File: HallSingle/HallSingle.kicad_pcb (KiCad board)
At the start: 2 copper layers, 12 x 24 mm, 11 parts, among them J1 Conn_01x03, U1 SS49E, U2 TS331ILT

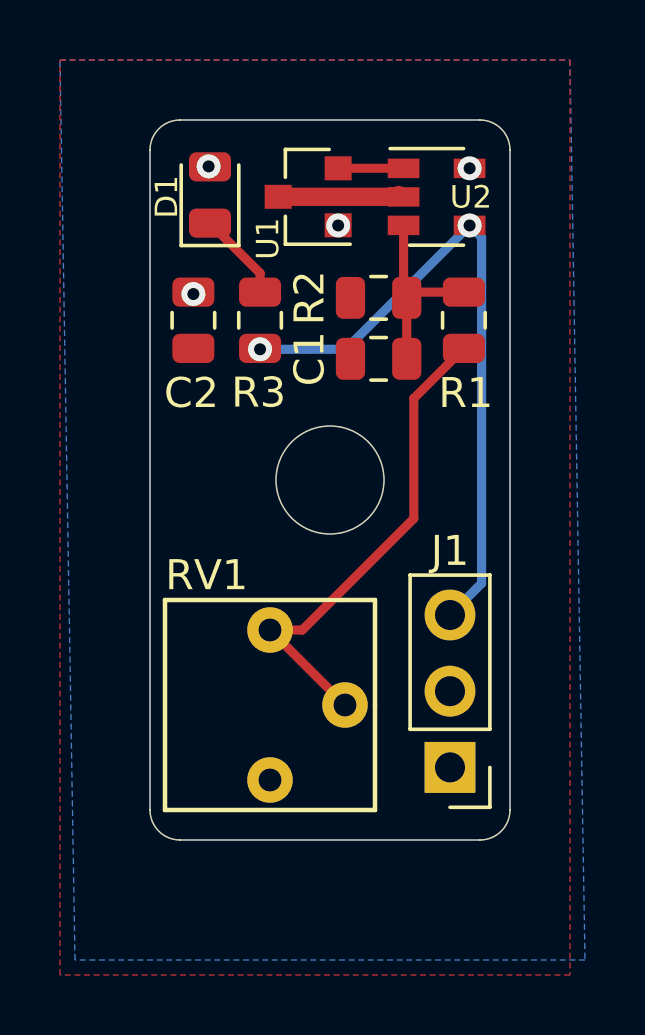
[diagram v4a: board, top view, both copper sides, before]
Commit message: actually reduce the pcb size this time....
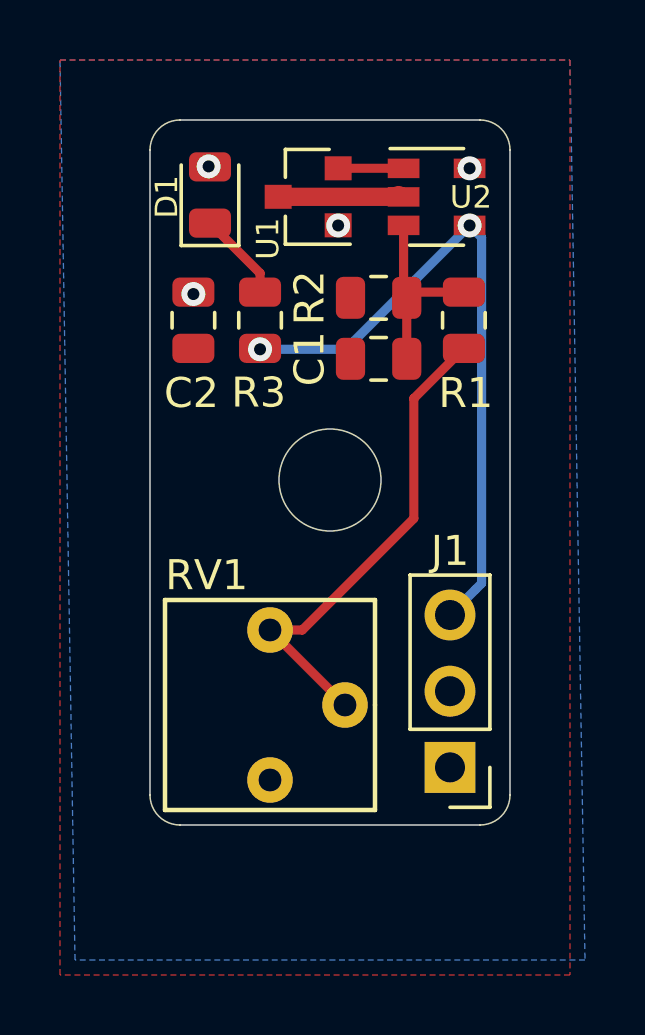
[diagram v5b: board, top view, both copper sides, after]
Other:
- board size 12 x 24 mm -> 12 x 23.5 mm
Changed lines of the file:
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@@
     (effects (font (size 1 1) (thickness 0.15)) (justify mirror))
   )
-  (gr_arc (start 139 80) (end 138 80) (angle -90) (layer Edge.Cuts) (width 0.05))
-  (gr_arc (start 149 80) (end 149 81) (angle -90) (layer Edge.Cuts) (width 0.05))
+  (gr_arc (start 139 79.5) (end 138 79.5) (angle -90) (layer Edge.Cuts) (width 0.05))
+  (gr_arc (start 149 79.5) (end 149 80.5) (angle -90) (layer Edge.Cuts) (width 0.05))
   (gr_arc (start 149 58) (end 150 58) (angle -90) (layer Edge.Cuts) (width 0.05))
   (gr_arc (start 139 58) (end 139 57) (angle -90) (layer Edge.Cuts) (width 0.05))
-  (gr_line (start 138 58) (end 138 80) (layer Edge.Cuts) (width 0.05))
-  (gr_line (start 149 81) (end 139 81) (layer Edge.Cuts) (width 0.05))
-  (gr_circle (center 144 69) (end 145.8 69) (layer Edge.Cuts) (width 0.05))
-  (gr_line (start 150 58) (end 150 80) (layer Edge.Cuts) (width 0.05))
+  (gr_line (start 138 58) (end 138 79.5) (layer Edge.Cuts) (width 0.05))
+  (gr_line (start 149 80.5) (end 139 80.5) (layer Edge.Cuts) (width 0.05))
+  (gr_circle (center 144 69) (end 145.7 69) (layer Edge.Cuts) (width 0.05))
+  (gr_line (start 150 58) (end 150 79.5) (layer Edge.Cuts) (width 0.05))
   (gr_line (start 139 57) (end 149 57) (layer Edge.Cuts) (width 0.05))
   (segment (start 146.284 59.5) (end 146.347 59.563) (width 0.6096) (layer F.Cu) (net 1))
@@
   (via (at 139.954 58.547) (size 0.8) (drill 0.4) (layers F.Cu B.Cu) (net 3))
   (via (at 144.272 60.5155) (size 0.8) (drill 0.4) (layers F.Cu B.Cu) (net 3))
-  (segment (start 143.07763 74) (end 142 74) (width 0.3048) (layer F.Cu) (net 6))
   (segment (start 141.6685 62.106) (end 140 60.4375) (width 0.3048) (layer F.Cu) (net 4))
   (segment (start 141.6685 62.738) (end 141.6685 62.106) (width 0.3048) (layer F.Cu) (net 4))
@@
   (segment (start 149.053499 72.446501) (end 148.849999 72.650001) (width 0.3048) (layer B.Cu) (net 5))
   (segment (start 148.6535 60.5155) (end 149.053499 60.915499) (width 0.3048) (layer B.Cu) (net 5))
+  (segment (start 143.07763 74) (end 142 74) (width 0.3048) (layer F.Cu) (net 6))
   (segment (start 148.463 64.613) (end 146.794399 66.281601) (width 0.3048) (layer F.Cu) (net 6))
   (segment (start 146.794399 66.281601) (end 146.794399 70.283231) (width 0.3048) (layer F.Cu) (net 6))

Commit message: Fixed Mounting hole
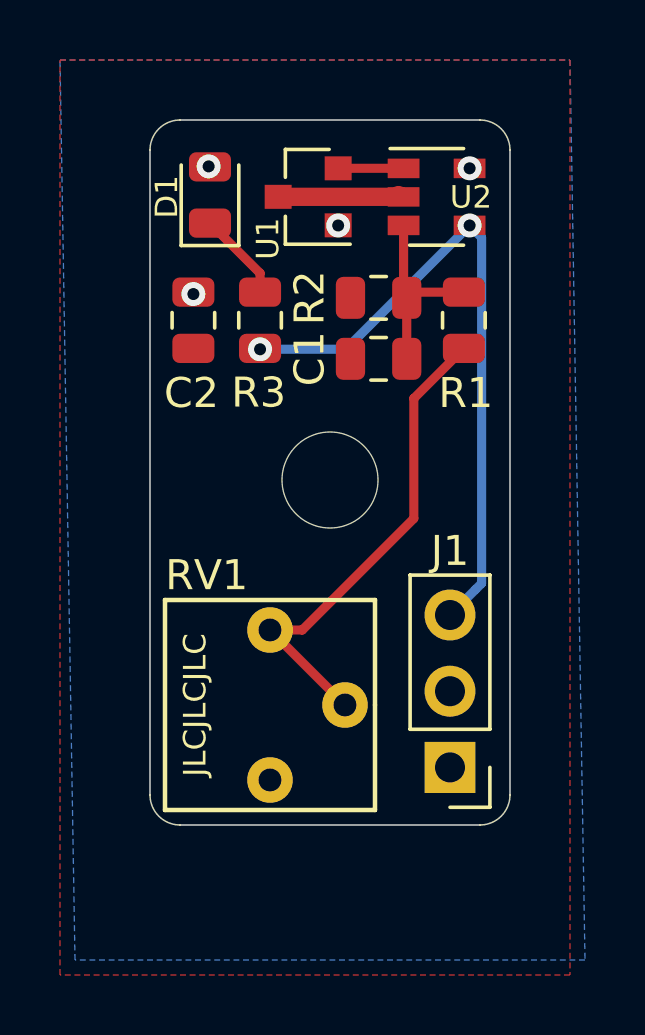
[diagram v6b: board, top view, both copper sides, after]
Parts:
- added REF**: MountingHole_3.2mm_M3, HallEffect:MountingHole_3.2mm_M3, F.Cu at (144.0, 69.0)
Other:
- outline, holes or cut-outs redrawn
- board text added: "JLCJLCJLC"
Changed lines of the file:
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@@
     (tracks 31)
     (zones 0)
-    (modules 11)
+    (modules 12)
     (nets 8)
   )
@@
     (add_net GND)
   )
+  (module HallEffect:MountingHole_3.2mm_M3 (layer F.Cu)
+    (at 144 69)
+    (descr "Mounting Hole 3.2mm, no annular, M3")
+    (tags "mounting hole 3.2mm no annular m3")
+    (attr virtual)
+    (fp_text reference REF** (at 0 0) (layer F.SilkS) hide
+      (effects (font (size 1 1) (thickness 0.15)))
+    )
+    (fp_text value MountingHole_3.2mm_M3 (at 0 4.2) (layer F.Fab)
+      (effects (font (size 1 1) (thickness 0.15)))
+    )
+    (fp_circle (center 0 0) (end 3.45 0) (layer F.CrtYd) (width 0.05))
+    (fp_circle (center 0 0) (end 3.2 0) (layer Cmts.User) (width 0.15))
+    (fp_text user %R (at 0.3 0) (layer F.Fab)
+      (effects (font (size 1 1) (thickness 0.15)))
+    )
+    (pad 1 np_thru_hole circle (at 0 0) (size 3.2 3.2) (drill 3.2) (layers *.Cu *.Mask))
+  )
   (module HallEffect:VoronLogo_6pt5mm_silkScreen (layer B.Cu)
     (at 144 61 270)
@@
     )
   )
+  (gr_text JLCJLCJLC (at 139.5 76.5 90) (layer F.SilkS)
+    (effects (font (size 0.75 0.75) (thickness 0.15)))
+  )
   (gr_text G (at 146.304 76.2) (layer B.SilkS)
     (effects (font (size 1 1) (thickness 0.15)) (justify mirror))
@@
   (gr_line (start 138 58) (end 138 79.5) (layer Edge.Cuts) (width 0.05))
   (gr_line (start 149 80.5) (end 139 80.5) (layer Edge.Cuts) (width 0.05))
-  (gr_circle (center 144 69) (end 145.7 69) (layer Edge.Cuts) (width 0.05))
   (gr_line (start 150 58) (end 150 79.5) (layer Edge.Cuts) (width 0.05))
   (gr_line (start 139 57) (end 149 57) (layer Edge.Cuts) (width 0.05))

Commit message: Remove JLC - doesnt fit with required sizing
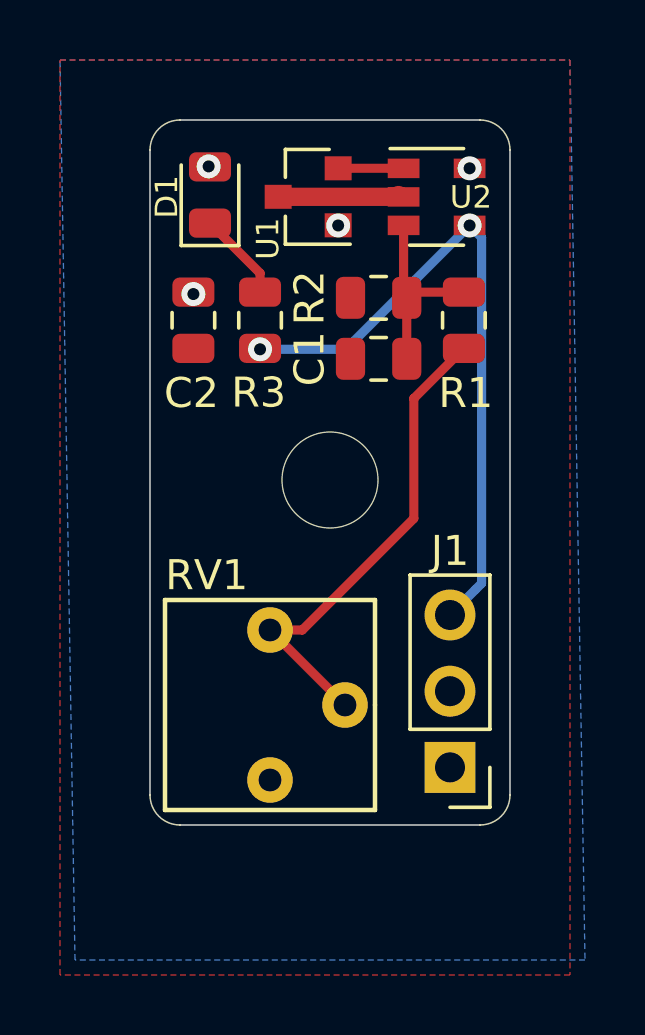
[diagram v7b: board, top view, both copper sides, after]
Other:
- board text removed: "JLCJLCJLC"
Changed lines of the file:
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@@
   (general
     (thickness 1.6)
-    (drawings 12)
+    (drawings 11)
     (tracks 31)
     (zones 0)
@@
     )
   )
-  (gr_text JLCJLCJLC (at 139.5 76.5 90) (layer F.SilkS)
-    (effects (font (size 0.75 0.75) (thickness 0.15)))
-  )
   (gr_text G (at 146.304 76.2) (layer B.SilkS)

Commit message: Updated with revision number. Corrected header orientation. added ibom
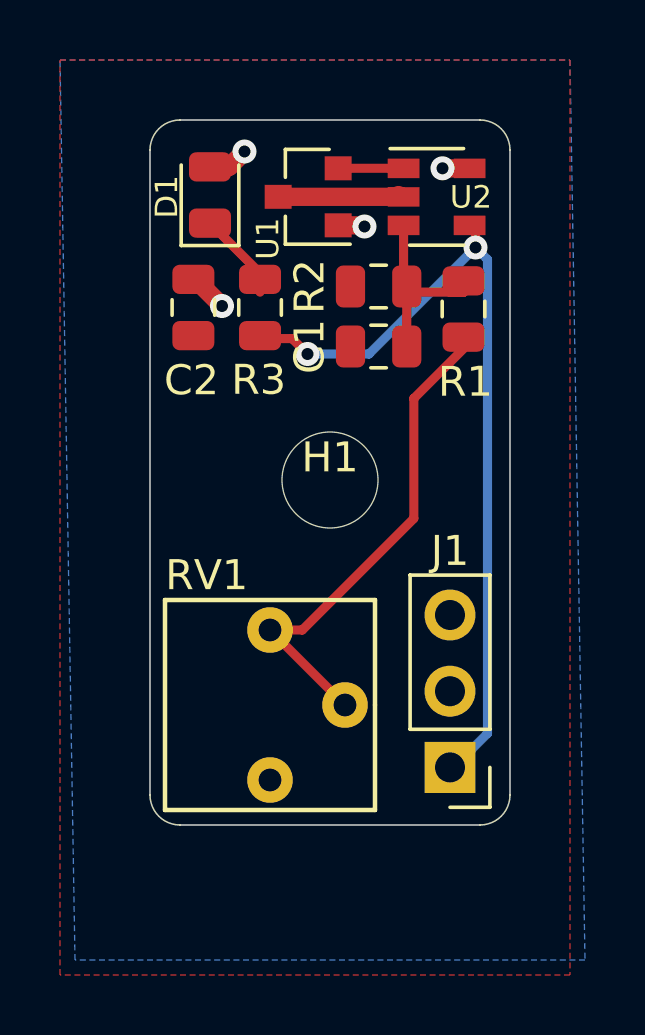
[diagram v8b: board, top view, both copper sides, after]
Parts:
- removed G***: LOGO, HallEffect:VoronLogo_6pt5mm_silkScreen
- removed REF**: MountingHole_3.2mm_M3, HallEffect:MountingHole_3.2mm_M3
- added H1: MountingHole, HallEffect:MountingHole_3.2mm_M3, F.Cu at (144.0, 69.0)
- moved C2 0.43 mm to (139.4, 63.2)
- moved R3 0.43 mm to (141.7, 63.2)
- moved C1 0.41 mm to (145.6, 64.5)
- moved R2 0.38 mm to (145.6, 62.5)
- moved R1 0.38 mm to (148.4, 63.3)
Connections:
- J1 pad 1: +5V -> Signal
- J1 pad 3: Signal -> +5V
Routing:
- net Signal: track 22.3 -> 27.8 mm
- net +5V: track 0.00 -> 4.44 mm
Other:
- board text added: "NO v1.0"
